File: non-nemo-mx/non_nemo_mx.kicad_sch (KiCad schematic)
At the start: 82 parts, among them J1 Conn_BAT, J2 Conn_BAT

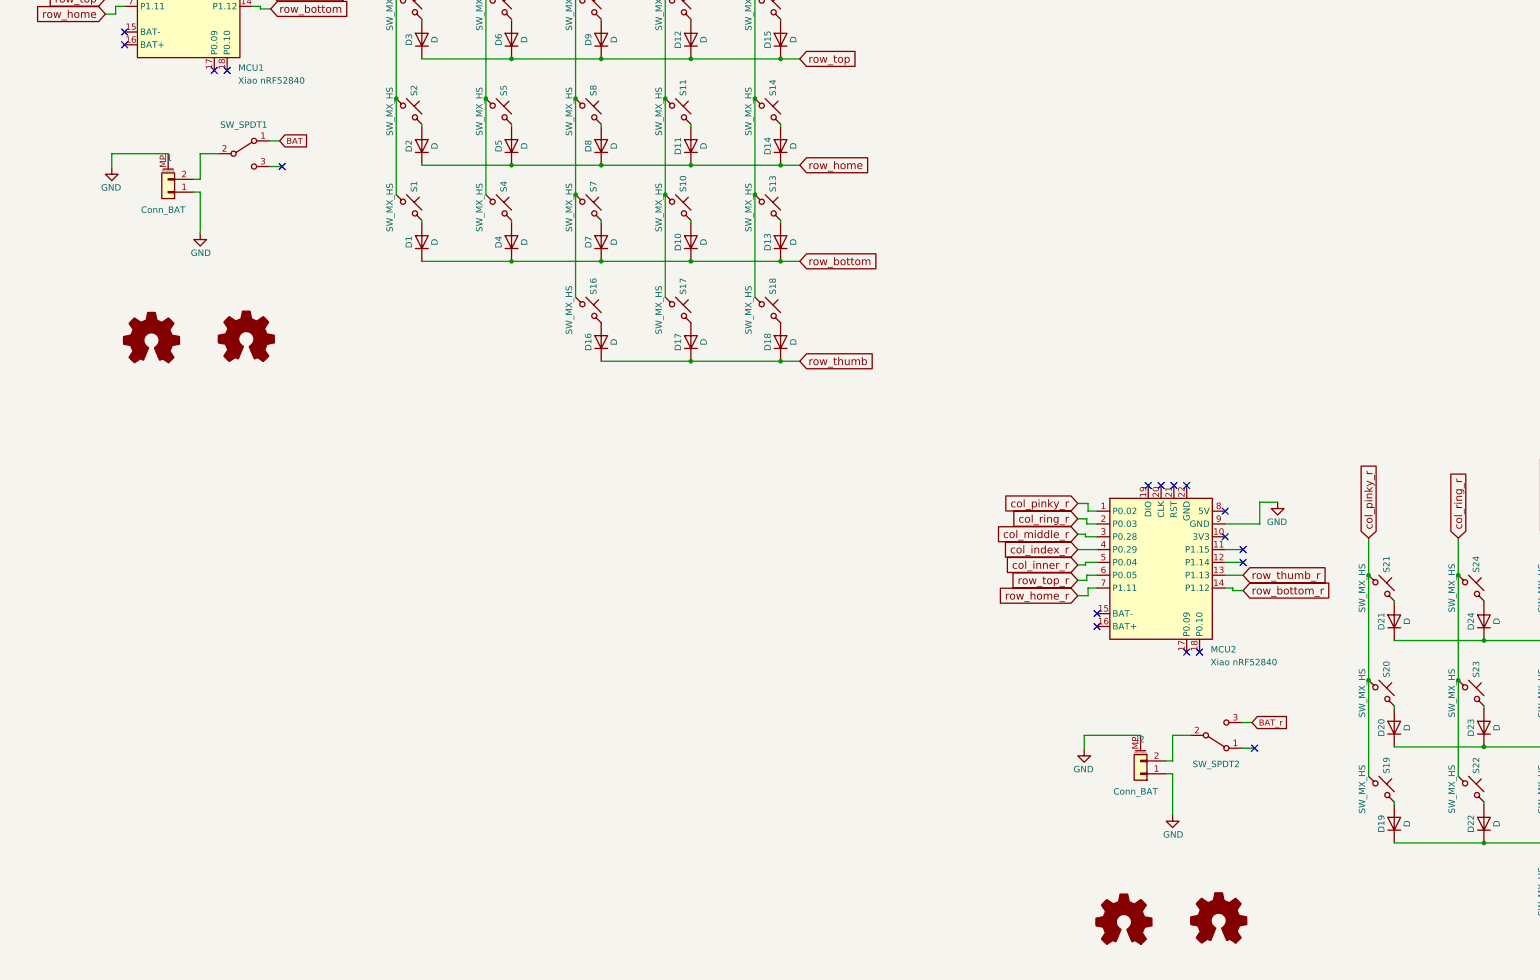
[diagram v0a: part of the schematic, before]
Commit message: reset switch (#6)
* added reset switch

* Low Profile

pogopin and reset button

* MX Profile

pogopin and reset switch

* MX Profile PCB

* Chimera

pogopin and reset switch

* version

* updated README.md
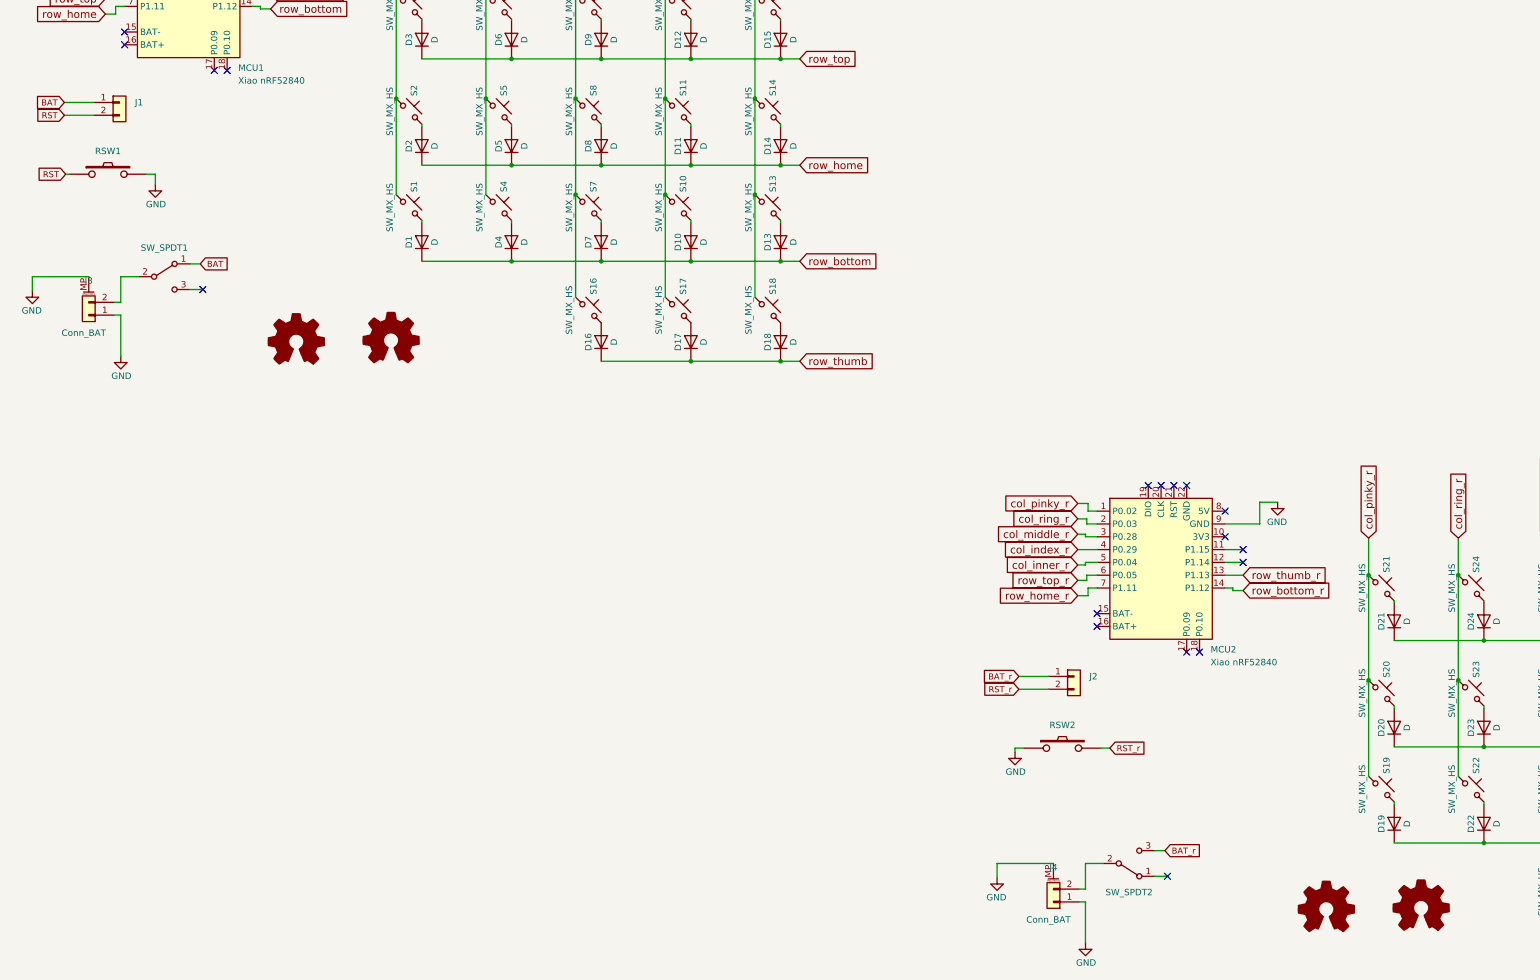
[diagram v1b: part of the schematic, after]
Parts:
- removed J1, J2: Conn_BAT, TB2086_SMD:Molex_Pico-EZmate_78171-0002_1x02-1MP_P1.20mm_HandSolder, symbol Connector_Generic_MountingPin:Conn_01x02_MountingPin
- added J1, J2: Conn_01x02, TB2086_MISC:Tag_Pogopin_1x02_P2.54mm, symbol Connector_Generic:Conn_01x02
- added J3, J4: Conn_BAT, TB2086_SMD:Molex_Pico-EZmate_78171-0002_1x02-1MP_P1.20mm_HandSolder, symbol Connector_Generic_MountingPin:Conn_01x02_MountingPin
- added RSW1, RSW2: SMT 2X4X3.5MM Tactile Tact Push Button, TB2086_SMD:SMT 2X4X3.5MM Tactile Tact Push Button, symbol TB2086_SMD:SMT 2X4X3.5MM Tactile Tact Push Button
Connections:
- net BAT: now also J1.1 (Pin_1)
- net BAT_r: now also J2.1 (Pin_1)
- net GND: now also J3.1 (Pin_1), J3.MP (MountPin), J4.1 (Pin_1), J4.MP (MountPin), RSW1.2, RSW2.1
- net at SW_SPDT2.2 (B): now also J4.2 (Pin_2)
- net at SW_SPDT1.2 (B): now also J3.2 (Pin_2)
- new net RST: J1.2 (Pin_2), RSW1.1
- new net RST_r: J2.2 (Pin_2), RSW2.2

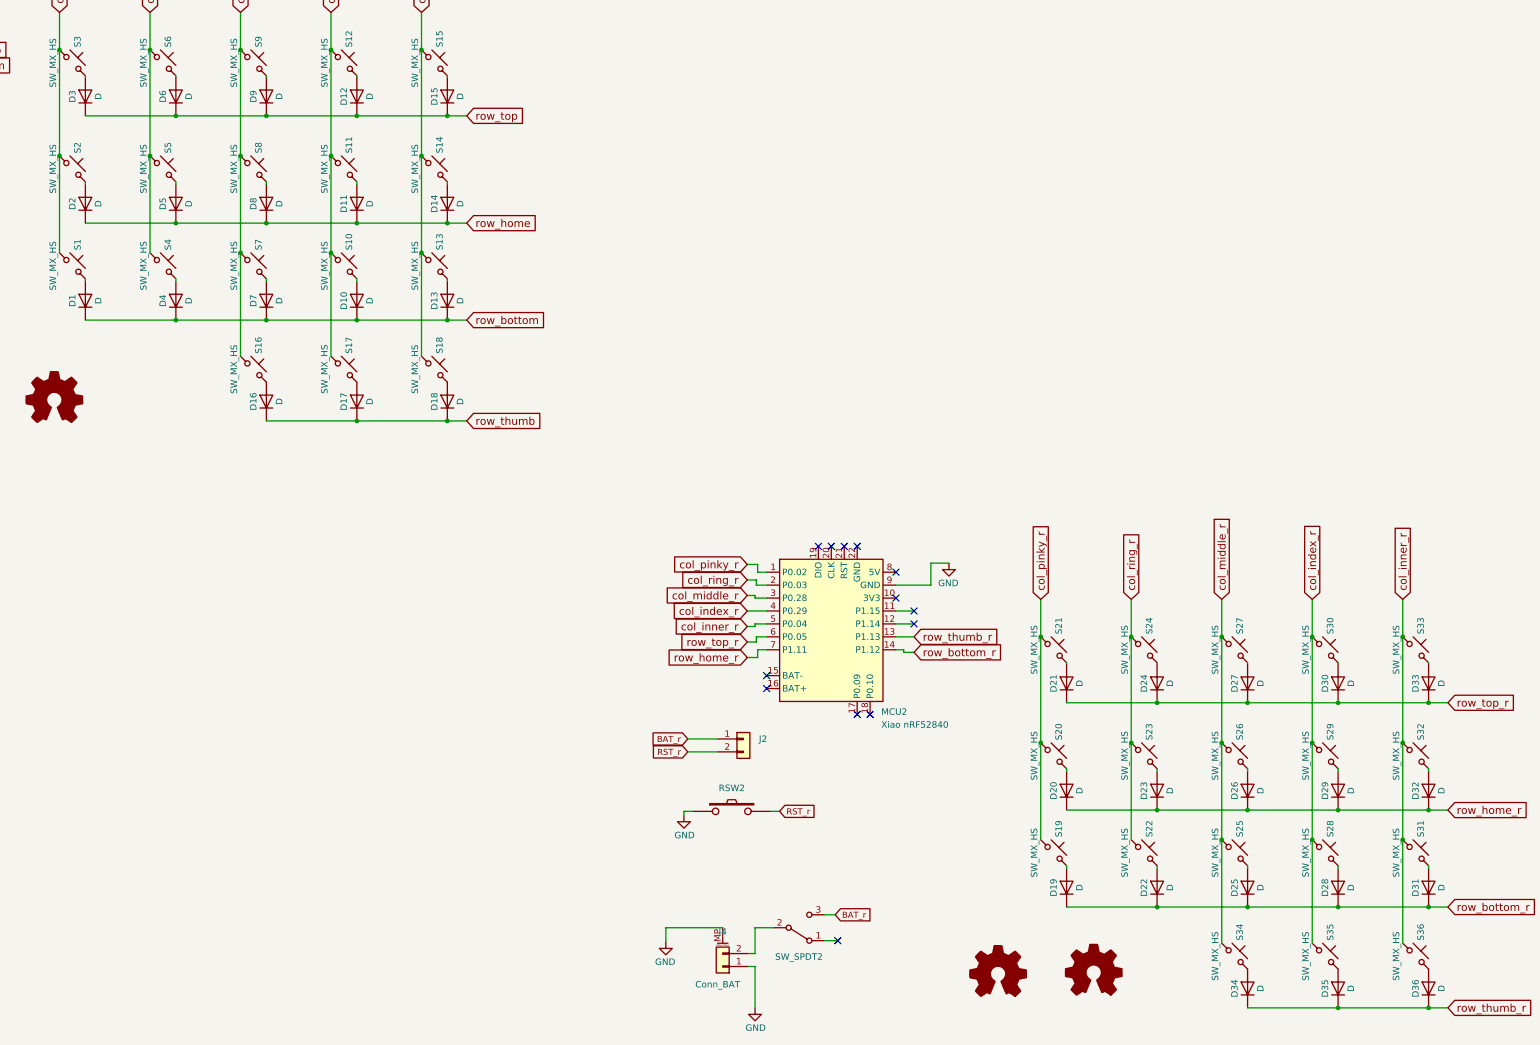
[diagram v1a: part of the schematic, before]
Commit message: fixed footprint layer for mx
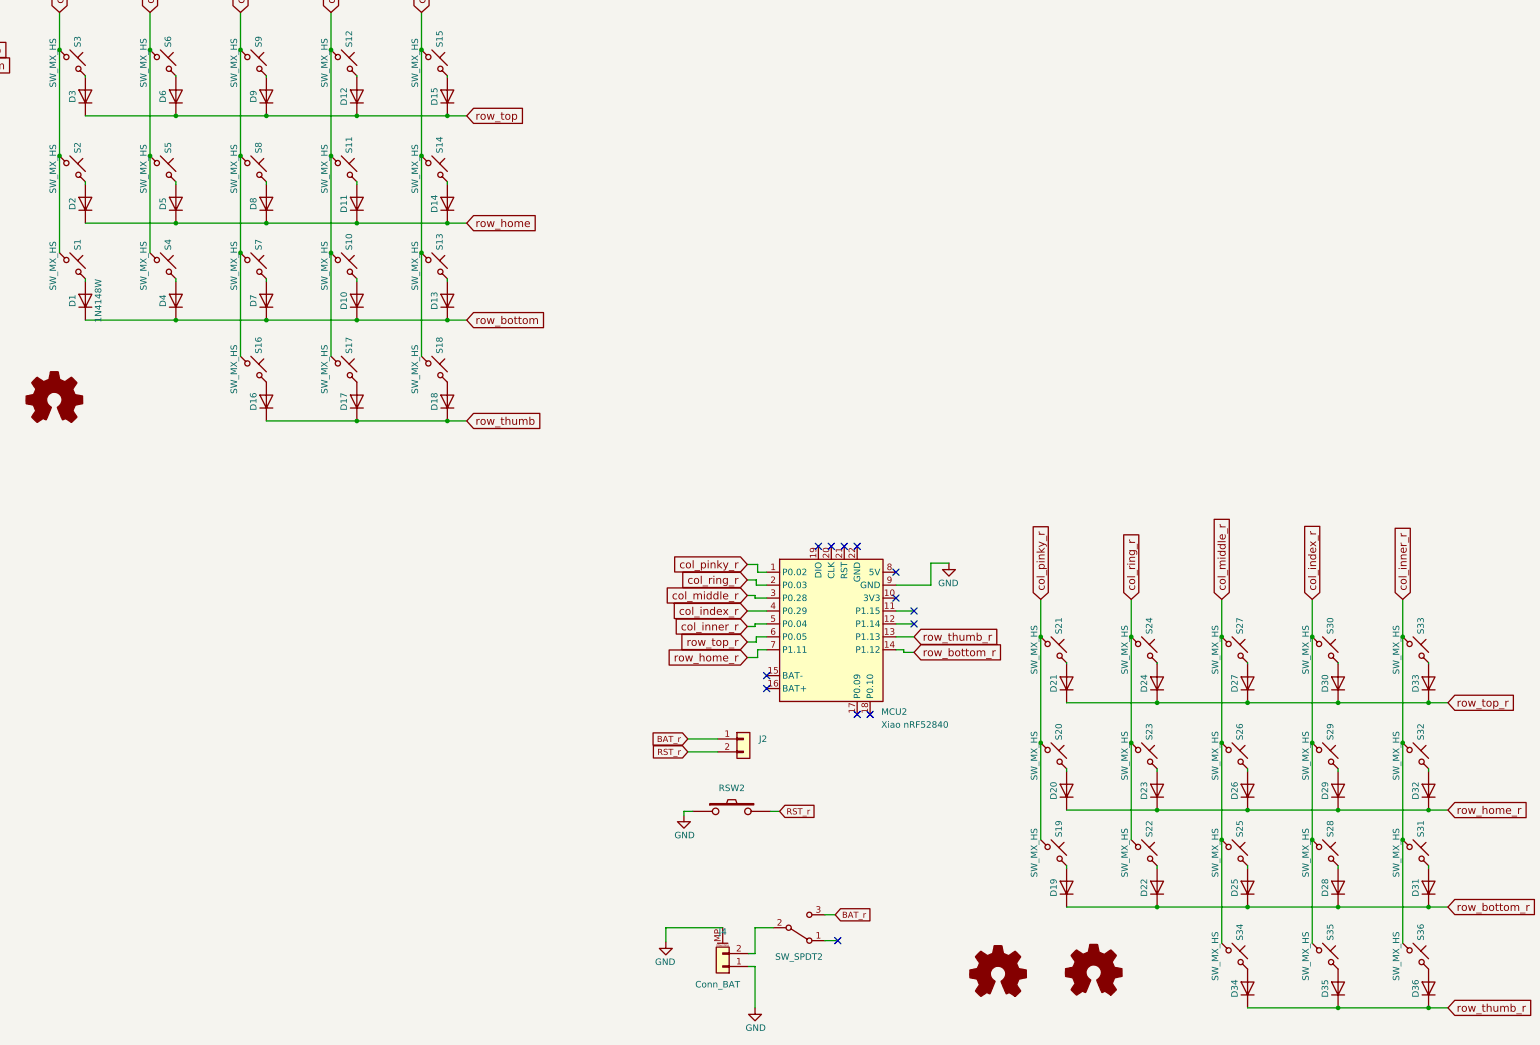
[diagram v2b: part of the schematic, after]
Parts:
- D1, D10, D11, D12, D13, D14, D15, D16, D17, D18, D19, D2, D20, D21, D22, D23, D24, D25, D26, D27, D28, D29, D3, D30, D31, D32, D33, D34, D35, D36, D4, D5, D6, D7, D8, D9: value D -> 1N4148W
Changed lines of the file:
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@@
 			)
 		)
-		(property "Value" "D"
+		(property "Value" "1N4148W"
 			(at 136.652 55.372 0)
 			(effects
@@
 					(size 1.27 1.27)
 				)
+					(hide yes)
 			)
 		)
@@
 			)
 		)
-		(property "Value" "D"
+		(property "Value" "1N4148W"
 			(at 329.438 170.688 0)
 			(effects
@@
 					(size 1.27 1.27)
 				)
+					(hide yes)
 			)
 		)
@@
 			)
 		)
-		(property "Value" "D"
+		(property "Value" "1N4148W"
 			(at 293.878 170.688 0)
 			(effects
@@
 					(size 1.27 1.27)
 				)
+					(hide yes)
 			)
 		)
@@
 			)
 		)
-		(property "Value" "D"
+		(property "Value" "1N4148W"
 			(at 118.872 76.454 0)
 			(effects
@@
 					(size 1.27 1.27)
 				)
+					(hide yes)
 			)
 		)
@@
 			)
 		)
-		(property "Value" "D"
+		(property "Value" "1N4148W"
 			(at 329.438 210.82 0)
 			(effects
@@
 					(size 1.27 1.27)
 				)
+					(hide yes)
 			)
 		)
@@
 			)
 		)
-		(property "Value" "D"
+		(property "Value" "1N4148W"
 			(at 118.872 55.372 0)
 			(effects
@@
 					(size 1.27 1.27)
 				)
+					(hide yes)
 			)
 		)
@@
 			)
 		)
-		(property "Value" "D"
+		(property "Value" "1N4148W"
 			(at 364.998 230.632 0)
 			(effects
@@
 					(size 1.27 1.27)
 				)
+					(hide yes)
 			)
 		)
@@
 			)
 		)
-		(property "Value" "D"
+		(property "Value" "1N4148W"
 			(at 118.872 95.504 0)
 			(effects
@@
 					(size 1.27 1.27)
 				)
+					(hide yes)
 			)
 		)
@@
 			)
 		)
-		(property "Value" "D"
+		(property "Value" "1N4148W"
 			(at 347.218 170.688 0)
 			(effects
@@
 					(size 1.27 1.27)
 				)
+					(hide yes)
 			)
 		)
@@
 			)
 		)
-		(property "Value" "D"
+		(property "Value" "1N4148W"
 			(at 364.998 170.688 0)
 			(effects
@@
 					(size 1.27 1.27)
 				)
+					(hide yes)
 			)
 		)
@@
 			)
 		)
-		(property "Value" "D"
+		(property "Value" "1N4148W"
 			(at 172.212 55.372 0)
 			(effects
@@
 					(size 1.27 1.27)
 				)
+					(hide yes)
 			)
 		)
@@
 			)
 		)
-		(property "Value" "D"
+		(property "Value" "1N4148W"
 			(at 154.432 95.504 0)
 			(effects
@@
 					(size 1.27 1.27)
 				)
+					(hide yes)
 			)
 		)
@@
 			)
 		)
-		(property "Value" "D"
+		(property "Value" "1N4148W"
 			(at 311.658 210.82 0)
 			(effects
@@
 					(size 1.27 1.27)
 				)
+					(hide yes)
 			)
 		)
@@
 			)
 		)
-		(property "Value" "D"
+		(property "Value" "1N4148W"
 			(at 136.652 95.504 0)
 			(effects
@@
 					(size 1.27 1.27)
 				)
+					(hide yes)
 			)
 		)
@@
 			)
 		)
-		(property "Value" "D"
+		(property "Value" "1N4148W"
 			(at 101.092 55.372 0)
 			(effects
@@
 					(size 1.27 1.27)
 				)
+					(hide yes)
 			)
 		)
@@
 			)
 		)
-		(property "Value" "D"
+		(property "Value" "1N4148W"
 			(at 172.212 115.316 0)
 			(effects
@@
 					(size 1.27 1.27)
 				)
+					(hide yes)
 			)
 		)
@@
 			)
 		)
-		(property "Value" "D"
+		(property "Value" "1N4148W"
 			(at 347.218 191.77 0)
 			(effects
@@
 					(size 1.27 1.27)
 				)
+					(hide yes)
 			)
 		)
@@
 			)
 		)
-		(property "Value" "D"
+		(property "Value" "1N4148W"
 			(at 154.432 55.372 0)
 			(effects
@@
 					(size 1.27 1.27)
 				)
+					(hide yes)
 			)
 		)
@@
 			)
 		)
-		(property "Value" "D"
+		(property "Value" "1N4148W"
 			(at 329.438 230.632 0)
 			(effects
@@
 					(size 1.27 1.27)
 				)
+					(hide yes)
 			)
 		)
@@
 			)
 		)
-		(property "Value" "D"
+		(property "Value" "1N4148W"
 			(at 364.998 191.77 0)
 			(effects
@@
 					(size 1.27 1.27)
 				)
+					(hide yes)
 			)
 		)
@@
 			)
 		)
-		(property "Value" "D"
+		(property "Value" "1N4148W"
 			(at 154.432 76.454 0)
 			(effects
@@
 					(size 1.27 1.27)
 				)
+					(hide yes)
 			)
 		)
@@
 			)
 		)
-		(property "Value" "D"
+		(property "Value" "1N4148W"
 			(at 154.432 115.316 0)
 			(effects
@@
 					(size 1.27 1.27)
 				)
+					(hide yes)
 			)
 		)
@@
 			)
 		)
-		(property "Value" "D"
+		(property "Value" "1N4148W"
 			(at 136.652 76.454 0)
 			(effects
@@
 					(size 1.27 1.27)
 				)
+					(hide yes)
 			)
 		)
@@
 			)
 		)
-		(property "Value" "D"
+		(property "Value" "1N4148W"
 			(at 172.212 76.454 0)
 			(effects
@@
 					(size 1.27 1.27)
 				)
+					(hide yes)
 			)
 		)
@@
 			)
 		)
-		(property "Value" "D"
+		(property "Value" "1N4148W"
 			(at 364.998 210.82 0)
 			(effects
@@
 					(size 1.27 1.27)
 				)
+					(hide yes)
 			)
 		)
@@
 			)
 		)
-		(property "Value" "D"
+		(property "Value" "1N4148W"
 			(at 172.212 95.504 0)
 			(effects
@@
 					(size 1.27 1.27)
 				)
+					(hide yes)
 			)
 		)
@@
 			)
 		)
-		(property "Value" "D"
+		(property "Value" "1N4148W"
 			(at 101.092 76.454 0)
 			(effects
@@
 					(size 1.27 1.27)
 				)
+					(hide yes)
 			)
 		)
@@
 			)
 		)
-		(property "Value" "D"
+		(property "Value" "1N4148W"
 			(at 293.878 210.82 0)
 			(effects
@@
 					(size 1.27 1.27)
 				)
+					(hide yes)
 			)
 		)
@@
 			)
 		)
-		(property "Value" "D"
+		(property "Value" "1N4148W"
 			(at 347.218 210.82 0)
 			(effects
@@
 					(size 1.27 1.27)
 				)
+					(hide yes)
 			)
 		)
@@
 			)
 		)
-		(property "Value" "D"
+		(property "Value" "1N4148W"
 			(at 136.652 115.316 0)
 			(effects
@@
 					(size 1.27 1.27)
 				)
+					(hide yes)
 			)
 		)
@@
 			)
 		)
-		(property "Value" "D"
+		(property "Value" "1N4148W"
 			(at 329.438 191.77 0)
 			(effects
@@
 					(size 1.27 1.27)
 				)
+					(hide yes)
 			)
 		)
@@
 			)
 		)
-		(property "Value" "D"
+		(property "Value" "1N4148W"
 			(at 347.218 230.632 0)
 			(effects
@@
 					(size 1.27 1.27)
 				)
+					(hide yes)
 			)
 		)
@@
 			)
 		)
-		(property "Value" "D"
+		(property "Value" "1N4148W"
 			(at 311.658 170.688 0)
 			(effects
@@
 					(size 1.27 1.27)
 				)
+					(hide yes)
 			)
 		)
@@
 			)
 		)
-		(property "Value" "D"
+		(property "Value" "1N4148W"
 			(at 293.878 191.77 0)
 			(effects
@@
 					(size 1.27 1.27)
 				)
+					(hide yes)
 			)
 		)
@@
 			)
 		)
-		(property "Value" "D"
+		(property "Value" "1N4148W"
 			(at 311.658 191.77 0)
 			(effects
@@
 					(size 1.27 1.27)
 				)
+				(hide yes)
 			)
 		)
@@
 			)
 		)
-		(property "Value" "D"
+		(property "Value" "1N4148W"
 			(at 101.092 95.504 0)
 			(effects
